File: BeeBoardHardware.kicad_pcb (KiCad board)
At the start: 2 copper layers, 48 parts, among them J1 Conn_01x10, J2 USB_C_Receptacle_USB2.0_16P, J3 Conn_01x02, Q1 AO3413, Q2 MMBT3904, Q3 MMBT3904, SW1 SW_Push, U1 MCP16311x-xMNY, U2 BQ24074RGT, U3 USBLC6-2SC6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

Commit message: organized pcb
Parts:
- removed Q1: AO3413, Package_TO_SOT_SMD:SOT-23
- added Q4: AO3413, Package_TO_SOT_SMD:SOT-23, F.Cu at (111.9, 65.9)
- added R21: 1k, Resistor_SMD:R_0402_1005Metric, F.Cu at (100.5, 80.5)
- moved H3 77.4 mm to (111.2, 90.0)
- moved D4 68.6 mm to (110.8, 73.8), turned to 180 degrees
- moved L1 68.1 mm to (103.8, 77.9), turned to 180 degrees
- moved H2 67.5 mm to (111.0, 51.2)
- moved R15 66.9 mm to (112.3, 73.2), turned to 90 degrees
- moved D3 66.2 mm to (108.5, 69.4), turned to -90 degrees
- moved Q3 64.8 mm to (113.4, 70.3), turned to 90 degrees
- moved R14 63.5 mm to (109.5, 69.4), turned to -90 degrees
- moved R5 63.0 mm to (101.8, 81.7), turned to 90 degrees
- moved R6 63.0 mm to (101.8, 83.6), turned to 90 degrees
- moved R12 61.0 mm to (109.3, 66.7), turned to -90 degrees
- moved C1 60.1 mm to (103.7, 84.9), turned to -90 degrees
- moved R11 59.8 mm to (106.0, 69.9), turned to 180 degrees
- moved R13 59.6 mm to (107.5, 69.4), turned to -90 degrees
- moved R8 59.3 mm to (90.6, 85.0), turned to -90 degrees
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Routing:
- added copper zone on B.Cu, net +3v3
- added copper zone on In1.Cu, net GND
- added copper zone on In2.Cu, net GND
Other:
- board outline added: 47 x 48 mm
- copper layers 2 -> 4
- board text added: "Bat Moniter"
- board text added: "CHARGER"
- board text added: "LATCH"
- board text added: "LMAKER"
- board text added: "USB"
- board text added: "Volt Reg"

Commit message: updated schematics and PCB
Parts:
- removed D3, D4: D, Diode_SMD:D_0402_1005Metric
- removed J1: Conn_01x10, Connector_PinHeader_2.54mm:PinHeader_1x10_P2.54mm_Vertical
- removed Q2, Q3: MMBT3904, Package_TO_SOT_SMD:SOT-23
- removed Q4: AO3413, Package_TO_SOT_SMD:SOT-23
- removed R11, R20: 220k, Resistor_SMD:R_0402_1005Metric
- removed R12, R14: 100k, Resistor_SMD:R_0402_1005Metric
- removed R13, R18: 10k, Resistor_SMD:R_0402_1005Metric
- removed R15: 220, Resistor_SMD:R_0402_1005Metric
- removed R19: 1k, Resistor_SMD:R_0402_1005Metric
- removed SW1: SW_Push, footprints:3983_switch
- added C10: 470n, Capacitor_SMD:C_0402_1005Metric, F.Cu at (99.8, 73.0)
- added C11: 1u, Capacitor_SMD:C_0402_1005Metric, F.Cu at (99.8, 71.9)
- added C12: 10n, Capacitor_SMD:C_0402_1005Metric, F.Cu at (99.8, 74.0)
- added C9: 100n, Capacitor_SMD:C_0402_1005Metric, F.Cu at (99.8, 70.9)
- added D5: LED, LED_SMD:LED_0402_1005Metric, F.Cu at (99.4, 82.6)
- added D7: LED, LED_SMD:LED_0402_1005Metric, F.Cu at (105.8, 74.2)
- added J4: Conn_01x11, Connector_PinHeader_2.54mm:PinHeader_1x11_P2.54mm_Vertical, F.Cu at (75.9, 58.1)
- added Q1: AO3413, Package_TO_SOT_SMD:SOT-23, F.Cu at (106.0, 68.3)
- added R22: 560, Resistor_SMD:R_0402_1005Metric, F.Cu at (104.8, 74.2)
- added R23: 10k, Resistor_SMD:R_0402_1005Metric, F.Cu at (105.1, 71.6)
- added SW2: SW_Push, footprints:3983_switch, F.Cu at (111.6, 71.7)
- added U5: STM6600DQ25DM6F, Package_DFN_QFN:TDFN-12_2x3mm_P0.5mm, F.Cu at (102.5, 72.1)
- R21: value 1k -> 10k
- moved R21 9.09 mm to (105.2, 72.7), turned to 180 degrees
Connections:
- R21 pad 1: +3v3 -> Net-(U5-~{PB}_OUT)
- R21 pad 2: GND -> PWR PTH

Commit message: setup all gnd vias and organized parts
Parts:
- moved D7 7.55 mm to (99.4, 70.3), turned to -90 degrees
- moved C9 6.77 mm to (105.4, 74.8), turned to 0 degrees
- moved C12 6.46 mm to (105.7, 71.3), turned to 0 degrees
- moved C11 6.04 mm to (105.7, 73.3), turned to 0 degrees
- moved C10 5.94 mm to (105.7, 72.3), turned to 0 degrees
- moved R22 5.84 mm to (100.4, 70.3), turned to 90 degrees
- moved J3 5.64 mm to (86.6, 64.3)
- moved R23 5.49 mm to (99.8, 72.8), turned to 180 degrees
- moved R21 5.43 mm to (99.8, 71.8)
- moved D2 4.98 mm to (84.1, 70.3), turned to 180 degrees
- moved D1 4.52 mm to (86.3, 69.8), turned to 180 degrees
- moved R10 4.29 mm to (90.7, 57.2)
- moved R17 4.29 mm to (90.7, 56.2)
- moved U4 4.13 mm to (86.8, 57.3)
- moved C8 3.28 mm to (83.6, 57.2), turned to 90 degrees
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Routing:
- net GND: track 0.00 -> 29.8 mm, vias 0 -> 28
- net BAT_SDA: track 0.00 -> 1.57 mm
- net BAT_SCL: track 0.00 -> 1.55 mm
- net BAT+: track 0.00 -> 1.31 mm
- removed copper zone on B.Cu, net +3v3
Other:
- board text added: "Bee Board"
- board text removed: "LMAKER"

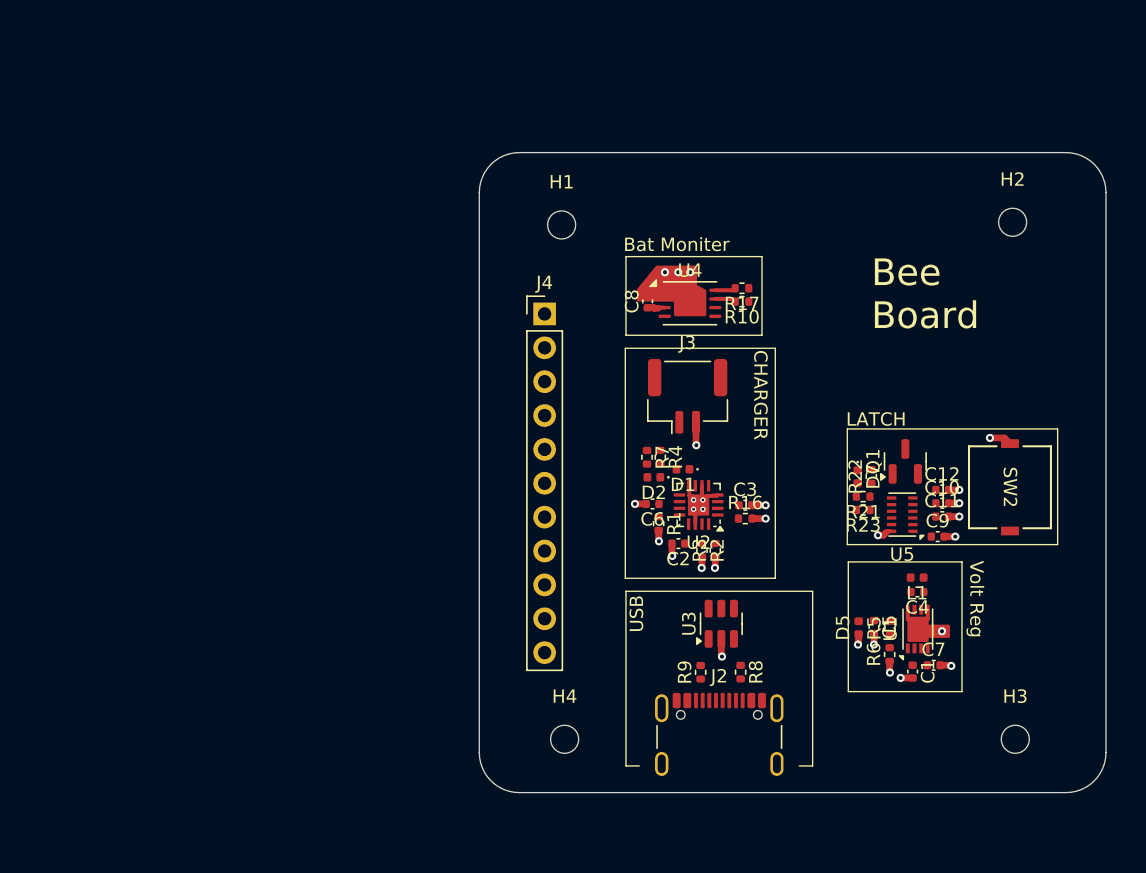
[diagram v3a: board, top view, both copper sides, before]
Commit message: routed more traces
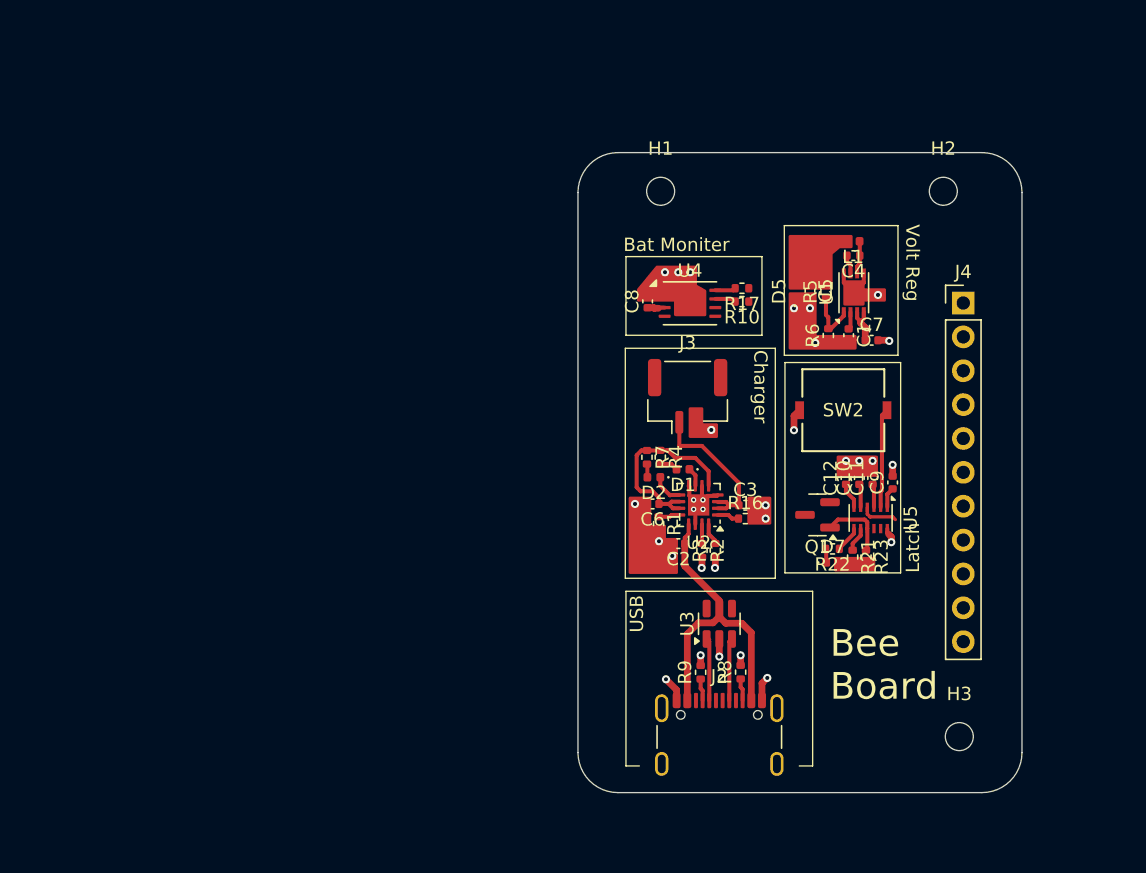
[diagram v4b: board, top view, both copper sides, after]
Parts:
- removed H4: MountingHole, MountingHole:MountingHole_2.1mm
- moved J4 31.4 mm to (107.3, 57.3)
- moved C4 25.7 mm to (99.1, 53.7)
- moved C5 25.7 mm to (95.8, 56.4)
- moved L1 25.7 mm to (99.0, 52.6)
- moved C1 25.7 mm to (98.7, 59.7)
- moved D5 25.7 mm to (94.7, 56.4)
- moved R5 25.7 mm to (97.0, 56.4)
- moved U1 25.7 mm to (99.1, 56.5)
- moved C7 24.8 mm to (100.4, 60.1)
- moved R6 24.4 mm to (97.2, 59.7)
- moved SW2 13.8 mm to (98.3, 65.3), turned to 0 degrees
- moved H1 7.84 mm to (84.6, 48.9)
- moved Q1 7.71 mm to (96.4, 73.2), turned to 180 degrees
- moved C12 7.28 mm to (98.5, 70.4), turned to 90 degrees
- moved D7 6.70 mm to (97.5, 76.7), turned to 0 degrees
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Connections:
- net Net-(J2-D+-PadA6) renamed PRE_D+
- net Net-(J2-D--PadA7) renamed PRE_D-
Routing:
- net VBUS: track 0.00 -> 24.7 mm
- net PWR PTH: track 0.00 -> 18.3 mm
- net BAT+: track 1.31 -> 13.0 mm
- net Net-(U5-~{PB}): track 0.00 -> 9.45 mm
- net +3v3: track 0.00 -> 6.79 mm
- net Net-(Q1-G): track 0.00 -> 5.27 mm
- net PRE_D-: track 0.00 -> 4.77 mm
- net PRE_D+: track 0.00 -> 4.70 mm
- net Net-(U1-Vfb): track 0.00 -> 4.17 mm
- net GND: track 29.8 -> 33.1 mm, vias 28 -> 31
- net PWR: track 0.00 -> 3.18 mm
- net LATCH: track 0.00 -> 2.78 mm
- net Net-(U1-SW): track 0.00 -> 2.50 mm
- net Net-(D2-K): track 0.00 -> 2.37 mm
- net Net-(U5-~{VCC}_LO): track 0.00 -> 1.98 mm
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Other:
- board size 47 x 48 mm -> 33.3 x 48 mm
- board text added: "Charger"
- board text added: "Latch"
- board text removed: "CHARGER"
- board text removed: "LATCH"

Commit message: routing headers next
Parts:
- removed H3: MountingHole, MountingHole:MountingHole_2.1mm
- U1: value MCP16311x-xMNY -> MCP16311T-E/MNY
- U2: value BQ24074RGT -> BQ24074RGTT
- moved H1 42.1 mm to (80.8, 90.8)
- moved C8 25.5 mm to (83.7, 82.7), turned to 180 degrees
- moved D5 24.3 mm to (73.5, 68.5)
- moved U1 24.3 mm to (77.9, 68.6)
- moved C4 24.3 mm to (77.9, 65.8)
- moved C5 24.3 mm to (74.7, 68.4)
- moved C1 24.3 mm to (77.6, 71.8)
- moved C7 24.3 mm to (79.3, 72.2)
- moved R5 24.3 mm to (75.9, 68.5)
- moved R6 24.3 mm to (76.0, 71.8)
- moved L1 24.3 mm to (77.9, 64.7)
- moved U4 22.4 mm to (83.8, 79.5), turned to 90 degrees
- moved H2 21.0 mm to (91.8, 64.6)
- moved R17 21.0 mm to (82.7, 75.6), turned to -90 degrees
- moved R10 19.7 mm to (83.7, 75.6), turned to -90 degrees
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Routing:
- net RST: track 0.00 -> 14.7 mm
- net PWR_DOWN: track 0.00 -> 11.9 mm
- net PWR: track 3.18 -> 13.3 mm
- net LATCH: track 2.78 -> 12.5 mm
- net BAT+: track 13.0 -> 17.1 mm
- net PWR PTH: track 18.3 -> 20.3 mm, vias 0 -> 2
- net BAT_ALERT: track 0.00 -> 1.61 mm, vias 0 -> 1
- net VBUS: track 24.7 -> 23.1 mm, vias 0 -> 2
- net Net-(U5-~{PB}): track 9.45 -> 10.8 mm
- net USB_D-: track 0.00 -> 1.22 mm, vias 0 -> 1
- net USB_D+: track 0.00 -> 1.22 mm, vias 0 -> 1
- net BAT_SCL: track 1.55 -> 2.68 mm, vias 0 -> 1
- net BAT_SDA: track 1.57 -> 2.57 mm, vias 0 -> 1
- net +3v3: track 6.79 -> 7.14 mm, vias 0 -> 1
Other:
- board size 33.3 x 48 mm -> 29.4 x 34.1 mm
- board text removed: "Bat Moniter"
- board text removed: "Charger"
- board text removed: "Latch"
- board text removed: "USB"
- board text removed: "Volt Reg"

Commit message: finish routes
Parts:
- moved R3 0.45 mm to (79.8, 87.3)
- moved R2 0.40 mm to (78.3, 88.0)
- moved H2 0.10 mm to (91.8, 64.7)
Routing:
- net PWR PTH: track 20.3 -> 62.6 mm, vias 2 -> 4
- net BAT_ALERT: track 1.61 -> 30.1 mm
- net VBUS: track 23.1 -> 48.4 mm
- net +3v3: track 7.14 -> 30.7 mm
- net BAT_SCL: track 2.68 -> 20.7 mm
- net BAT_SDA: track 2.57 -> 17.5 mm
- net USB_D-: track 1.22 -> 12.0 mm
- net USB_D+: track 1.22 -> 9.00 mm
- net GND: track 33.2 -> 38.2 mm, vias 31 -> 29
- net Net-(U5-~{PB}): track 10.8 -> 15.0 mm
- net PWR: track 13.3 -> 14.1 mm
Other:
- board size 29.4 x 34.1 mm -> 29.4 x 32.9 mm
